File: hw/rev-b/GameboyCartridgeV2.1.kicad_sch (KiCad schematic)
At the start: 0 parts

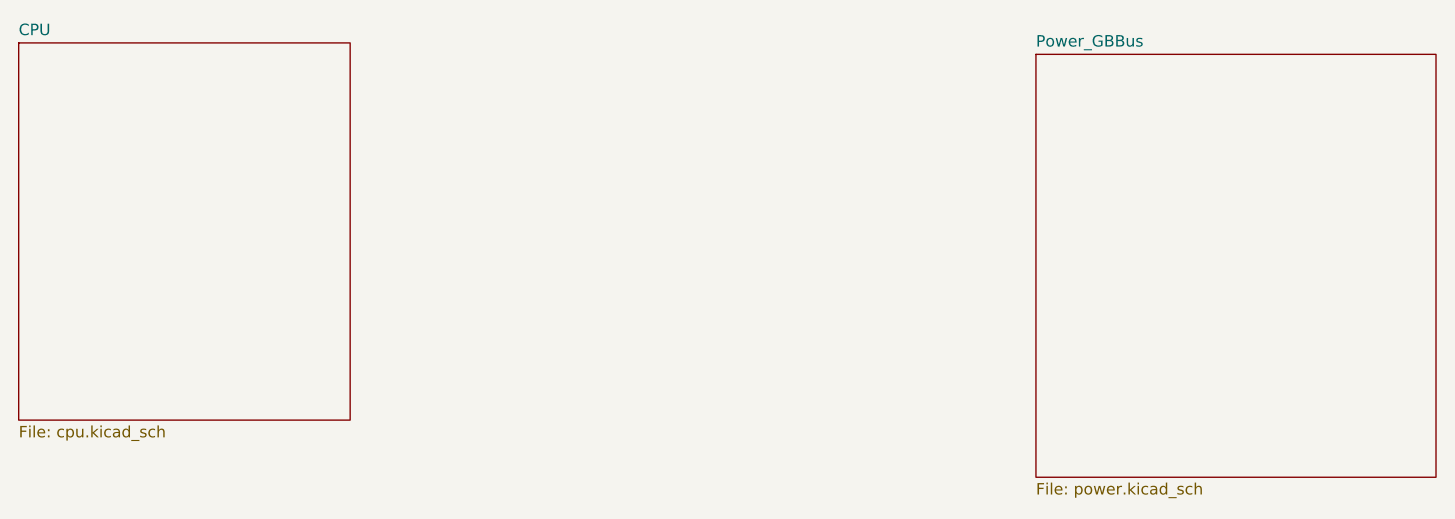
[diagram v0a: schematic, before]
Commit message: schematic: radio sheet in the KiCad project (symbol lib generator, Croco edits applied + verified, PWR_FLAG, layout), KiCad lib env + re-recorded baseline, checker fixes (length-normalised fingerprints, accepted list, Radio sheet excluded from Croco netlist); logbook
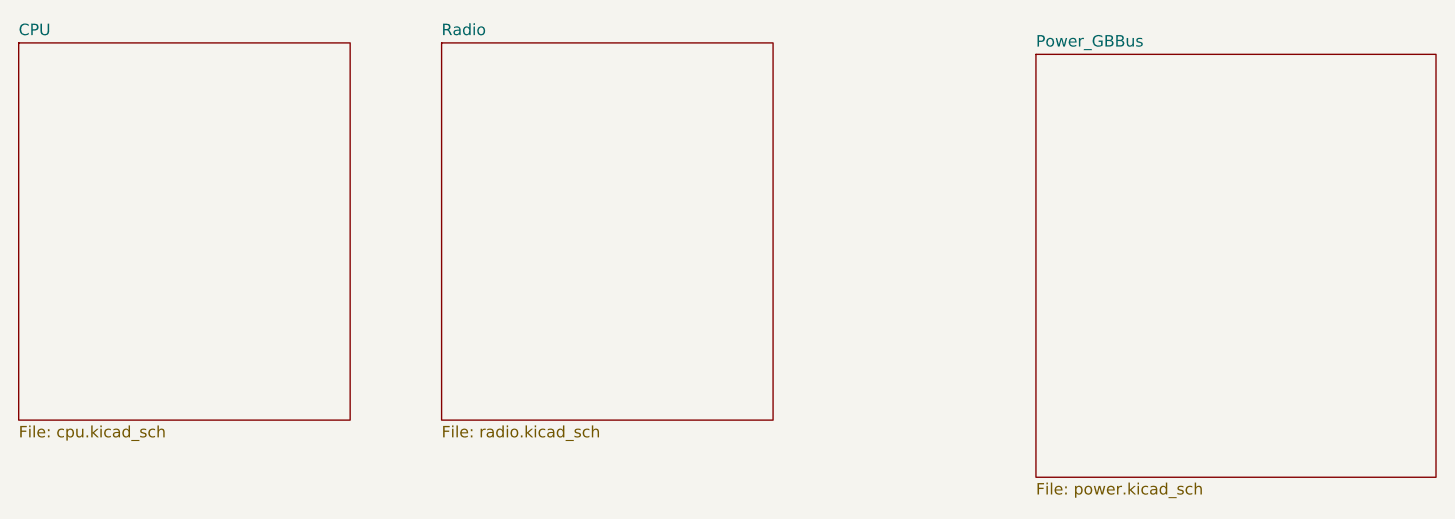
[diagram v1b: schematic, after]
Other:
- added sheet Radio (radio.kicad_sch)
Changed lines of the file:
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@@
+		)
+	)
+	(sheet
+		(at 101.6 57.15)
+		(size 36.83 41.91)
+		(exclude_from_sim no)
+		(in_bom yes)
+		(on_board yes)
+		(dnp no)
+		(fields_autoplaced yes)
+		(stroke
+			(width 0.1524)
+			(type solid)
+		)
+		(fill
+			(color 0 0 0 0.0000)
+		)
+		(property "Sheetname" "Radio"
+			(at 101.6 56.4384 0)
+			(effects
+				(font
+					(size 1.27 1.27)
+				)
+				(justify left bottom)
+			)
+		)
+		(property "Sheetfile" "radio.kicad_sch"
+			(at 101.6 99.6446 0)
+			(effects
+				(font
+					(size 1.27 1.27)
+				)
+				(justify left top)
+			)
+		)
+		(instances
+			(project "GameboyCartridgeV2.1"
+				(path "/ec16e1da-c950-4911-941a-a1ab0200cc01"
+					(page "4")
+				)
+			)
 		)
 	)
